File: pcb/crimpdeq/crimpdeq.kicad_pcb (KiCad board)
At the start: 2 copper layers, 23 x 63.8 mm, 48 parts, among them J2 USB4105-GF-A, J3 Loadcell_Pads, J4 Power_Sense_Pads, Q1 SS8550, Q2 DMG3415U, U1 ESP32-C3-MINI-1, U2 MCP73831T-2ACI/OT, U3 HX711, U5 MAX17048G+T10, U6 SY8088

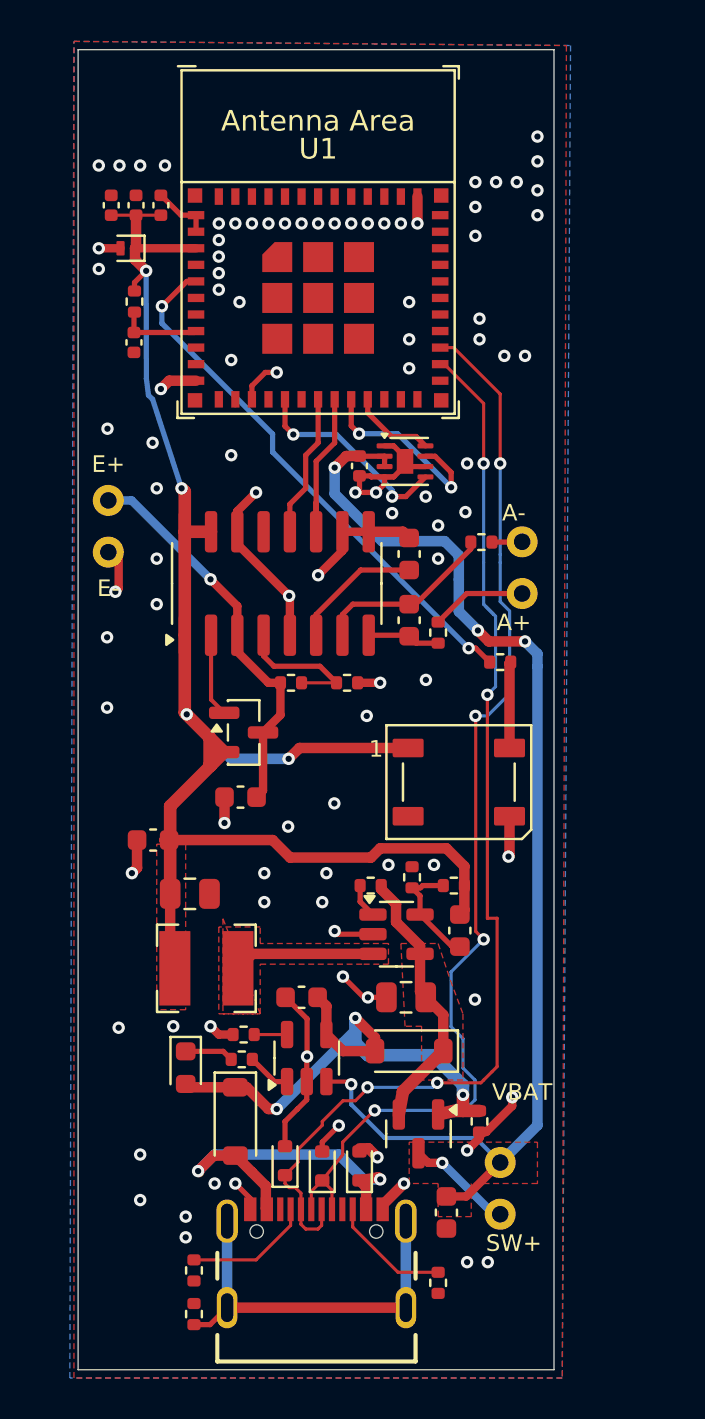
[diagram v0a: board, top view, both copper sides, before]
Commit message: Revision 3 (#26)
* Reorganize PCB designs and add crimpdeq-v2-nano (25x26mm 4-layer compact board)

Moves the original design to pcb/designs/crimpdeq-v2/ so each PCB
package can live in its own versioned directory, and adds
pcb/designs/crimpdeq-v2-nano/: a 4-layer, 25 x 26 mm redesign
(~56% smaller board area than crimpdeq-v2: 1467.4 mm2 -> 650.0 mm2)
with the ESP32 antenna and status LED both moved to the back and
USB/HX711 kept on the front.

- Electrically identical to crimpdeq-v2: same 48-component BOM,
  same 197-pad netlist, 0 changed nets
- Passes KiCad DRC (0 violations, 0 unconnected)
- Validated on JLCPCB's website DFM checker: all danger-level
  findings were reviewed and resolved before committing (functional-
  label silk-to-pad/hole clearances, tht-to-smd cable pad gaps,
  USB-C shell slot width). Only conservative warning-level advisories
  remain on the six 1.50 mm cable PTH pads and the USB shell slot
  (see reports/crimpdeq-v2-nano_jlc_tht_to_smd.md)
- Updates the CI matrix to check both designs

Physical prototype validation of antenna performance and connector
fit is still pending.

* Add agents.md and 4-layer/compact reproduction tooling, symlink CLAUDE.md

agents.md documents the frozen BOM/netlist/routing invariants and
session history for the crimpdeq-v2 / crimpdeq-v2-nano designs.
tools/4layer/ and tools/compact/ are the scripted place -> route ->
verify pipeline used to build and DFM-check crimpdeq-v2-nano from
the crimpdeq-v2 baseline. CLAUDE.md is a symlink to agents.md for
AI coding agents that look for that filename by convention.

* fix: prepare nano project for release

* test: lock corrected PCB connectivity

Validate every connected pad against the revised golden netlist so ESP32 ground-pin and pull-up regressions fail immediately.

Co-authored-by: Cursor <cursoragent@cursor.com>

* refactor: consolidate the canonical PCB package

Move shared libraries to the repository root and replace versioned design trees with the corrected prod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
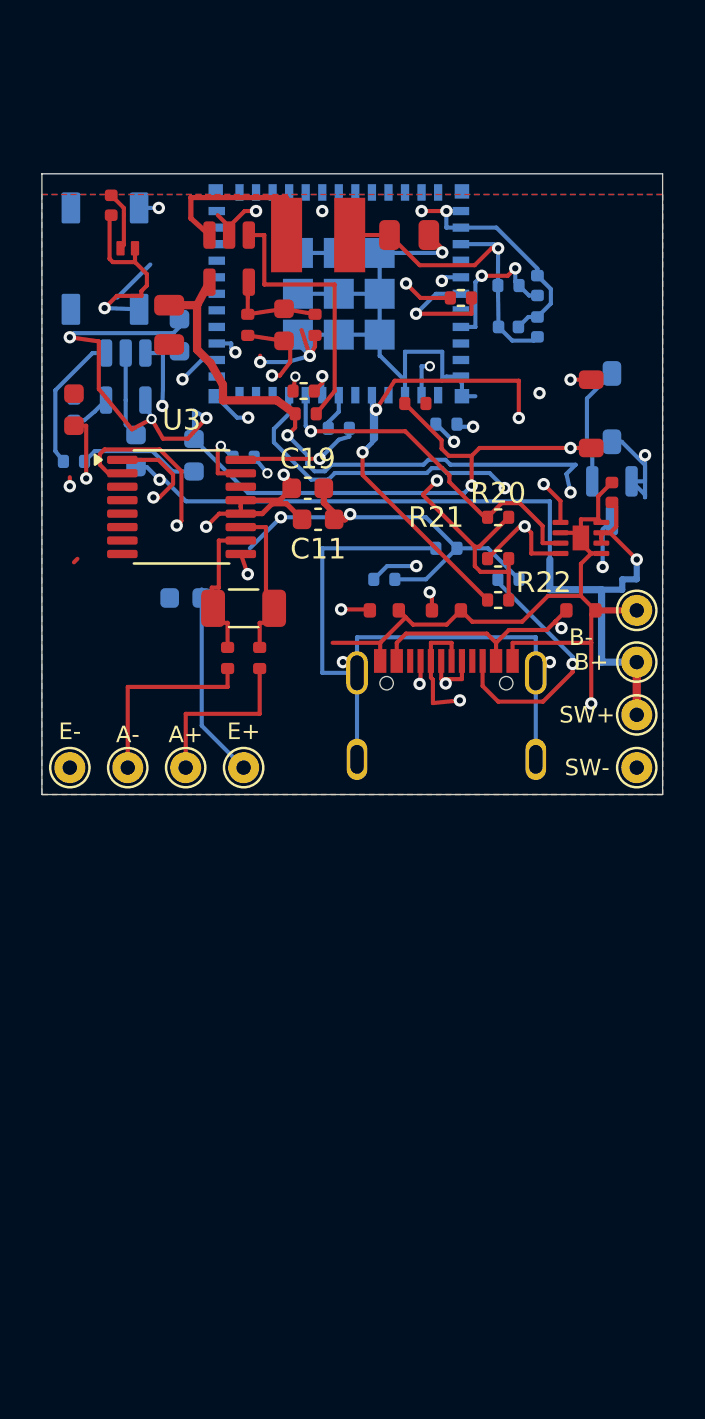
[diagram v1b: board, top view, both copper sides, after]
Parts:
- removed J3: Loadcell_Pads, External_Cable_Pads_Left
- removed J4: Power_Sense_Pads, External_Cable_Pads_Right
- removed Q1: SS8550, Package_TO_SOT_SMD:SOT-23
- removed R5: 12kR 1%, Resistor_SMD:R_0402_1005Metric
- removed R6: 8k2R 1%, Resistor_SMD:R_0402_1005Metric
- added C19: 0.1uF, Capacitor_SMD:C_0603_1608Metric, F.Cu at (140.3, 67.6)
- added J10: A-_Cable_Pad, TestPoint:TestPoint_THTPad_D1.5mm_Drill0.7mm, F.Cu at (131.6, 81.1)
- added J11: E+_Cable_Pad, TestPoint:TestPoint_THTPad_D1.5mm_Drill0.7mm, F.Cu at (137.2, 81.1)
- added J12: E-_Cable_Pad, TestPoint:TestPoint_THTPad_D1.5mm_Drill0.7mm, F.Cu at (128.8, 81.1)
- added J5: B-_Cable_Pad, TestPoint:TestPoint_THTPad_D1.5mm_Drill0.7mm, F.Cu at (156.2, 73.5)
- added J6: SW+_Cable_Pad, TestPoint:TestPoint_THTPad_D1.5mm_Drill0.7mm, F.Cu at (156.2, 78.5)
- added J7: B+_Cable_Pad, TestPoint:TestPoint_THTPad_D1.5mm_Drill0.7mm, F.Cu at (156.2, 76.0)
- added J8: SW-_Cable_Pad, TestPoint:TestPoint_THTPad_D1.5mm_Drill0.7mm, F.Cu at (156.2, 81.1)
- added J9: A+_Cable_Pad, TestPoint:TestPoint_THTPad_D1.5mm_Drill0.7mm, F.Cu at (134.4, 81.1)
- added R20: 10kR 1%, Resistor_SMD:R_0402_1005Metric, F.Cu at (149.5, 69.0)
- added R21: 10kR 1%, Resistor_SMD:R_0402_1005Metric, F.Cu at (149.5, 71.0)
- added R22: 10kR 1%, Resistor_SMD:R_0402_1005Metric, F.Cu at (149.5, 73.0)
- added R23: 47R 1%, Resistor_SMD:R_0402_1005Metric, F.Cu at (140.1, 62.9)
- added R24: 47R 1%, Resistor_SMD:R_0402_1005Metric, B.Cu at (141.8, 64.7)
- added R25: 47R 1%, Resistor_SMD:R_0402_1005Metric, F.Cu at (147.7, 58.4)
- added R26: 47R 1%, Resistor_SMD:R_0402_1005Metric, B.Cu at (137.2, 66.1)
- C1, C10, C2, C3, C5, C6, D1, D2, D4, R1, R13, R17, R18, R19, R2, R3: moved to B.Cu
- C12: footprint Capacitor_SMD:C_0603_1608Metric -> Capacitor_SMD:C_1206_3216Metric
- J2: footprint Rust_Board:GCT_USB4105-GF-A -> Crimpdeq:GCT_USB4105-GF-A
- Q2: footprint Package_TO_SOT_SMD:SOT-23 -> Crimpdeq:SOT-23; moved to B.Cu
- U1: footprint PCM_Espressif:ESP32-C3-MINI-1 -> Crimpdeq:ESP32-C3-MINI-1; moved to B.Cu
- U2: footprint Package_TO_SOT_SMD:SOT-23-5 -> Crimpdeq:MCP73831_SOT-23-5; moved to B.Cu
- U3: value HX711 -> ADS1220; footprint Package_SO:SOP-16_3.9x9.9mm_P1.27mm -> Package_SO:TSSOP-16_4.4x5mm_P0.65mm
- U6: footprint Package_TO_SOT_SMD:SOT-23-5 -> Crimpdeq:SY8088_SOT-23-5
- moved C6 39.7 mm to (132.0, 65.8), turned to 90 degrees
- moved R17 39.0 mm to (147.0, 70.5), turned to 0 degrees
- moved D8 38.3 mm to (154.0, 64.0), turned to 90 degrees
- moved L1 35.8 mm to (140.8, 55.4), turned to 0 degrees
- moved R9 34.8 mm to (145.5, 63.5), turned to 0 degrees
- moved R19 34.6 mm to (144.0, 72.0), turned to 0 degrees
- moved C15 34.5 mm to (133.6, 59.7), turned to -90 degrees
- moved R18 34.2 mm to (150.0, 72.0), turned to 0 degrees
- moved U2 34.1 mm to (131.5, 62.2), turned to -90 degrees
- moved U6 33.6 mm to (136.5, 56.5), turned to -90 degrees
- moved C17 33.6 mm to (145.2, 55.4)
- moved D2 32.6 mm to (155.0, 63.7), turned to 90 degrees
- moved C5 32.5 mm to (134.1, 60.2), turned to 90 degrees
- moved Q2 32.0 mm to (155.0, 68.2)
- moved R2 31.3 mm to (129.0, 63.8), turned to -90 degrees
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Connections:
- net /Buck_Coil renamed Buck_Coil
- net IO6_SDA renamed IO6_SCL
- net IO7_SCL renamed IO7_SDA
- C10 pad 1: E+ -> +3V3
- C11 pad 1: GND -> +3V3
- C11 pad 2: Net-(U3-VBG) -> GND
- C12 pad 1: Net-(U3-INA+) -> Net-(U3-AIN0)
- C12 pad 2: Net-(U3-INA-) -> Net-(U3-AIN1)
- R7 pad 1: Net-(U3-INA+) -> Net-(U3-AIN0)
- R8 pad 1: Net-(U3-INA-) -> Net-(U3-AIN1)
- U1 pad 13: unconnected-(U1-GPIO1/ADC1_CH1/XTAL_32K_N-Pad13) -> IO1_MISO
- U1 pad 18: IO4_DATA -> IO4_MOSI
- U1 pad 37: (no net) -> GND
- U1 pad 38: (no net) -> GND
- U1 pad 39: (no net) -> GND
- U1 pad 40: (no net) -> GND
- U1 pad 41: (no net) -> GND
- U1 pad 42: (no net) -> GND
- U1 pad 43: (no net) -> GND
- U1 pad 44: (no net) -> GND
- U1 pad 45: (no net) -> GND
- U1 pad 46: (no net) -> GND
- U1 pad 47: (no net) -> GND
- U1 pad 48: (no net) -> GND
- U1 pad 49: (no net) -> GND
- U1 pad 50: (no net) -> GND
- U1 pad 51: (no net) -> GND
- U1 pad 52: (no net) -> GND
- U1 pad 53: (no net) -> GND
- U1 pad 6: unconnected-(U1-GPIO3/ADC1_CH3-Pad6) -> IO3_CS
- U3 pad 1: +3V3 -> ADS_SCLK
- U3 pad 10: GND -> Net-(U3-AIN1)
- U3 pad 11: IO5_SCK -> Net-(U3-AIN0)
- U3 pad 12: IO4_DATA -> +3V3
- U3 pad 13: unconnected-(U3-XO-Pad13) -> +3V3
- U3 pad 14: GND -> unconnected-(U3-~{DRDY}-Pad14)
- U3 pad 15: +3V3 -> ADS_DOUT
- U3 pad 16: +3V3 -> ADS_DIN
- U3 pad 2: Net-(Q1-B) -> ADS_CS
- U3 pad 3: E+ -> GND
- U3 pad 4: Net-(U3-VFB) -> GND
- U3 pad 6: Net-(U3-VBG) -> unconnected-(U3-AIN3/REFN1-Pad6)
- U3 pad 7: Net-(U3-INA-) -> unconnected-(U3-AIN2-Pad7)
- U3 pad 8: Net-(U3-INA+) -> GND
- U3 pad 9: GND -> +3V3
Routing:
- net GND: track 63.5 -> 137.2 mm, vias 98 -> 13
- net +3V3: track 78.2 -> 116.5 mm, vias 4 -> 8
- net ADS_CS: track 0.00 -> 35.8 mm, vias 0 -> 2
- net Net-(D4-DIN): track 4.17 -> 31.1 mm, vias 0 -> 2
- net VSYS: track 13.1 -> 39.9 mm, vias 0 -> 3
- net VBUS: track 28.3 -> 53.1 mm, vias 3 -> 5
- net IO1_MISO: track 0.00 -> 24.0 mm, vias 0 -> 2
- net ADS_SCLK: track 0.00 -> 21.1 mm, vias 0 -> 2
- net IO10_ALRT: track 10.1 -> 30.0 mm, vias 2 -> 4
- net E+: track 19.9 -> 0.00 mm, vias 1 -> 0
- net IO7_SDA: track 4.10 -> 22.7 mm, vias 0 -> 2
- net Net-(J2-SHELL_GND-PadS1): track 18.9 -> 35.0 mm, vias 0 -> 2
- net IO2_LED: track 26.1 -> 10.2 mm
- net USB_D+: track 53.3 -> 37.7 mm, vias 4 -> 3
- net USB_D-: track 54.1 -> 40.2 mm, vias 4 -> 3
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- added copper zone on In2.Cu, net +3V3
- added copper zone on In1.Cu, net GND
- removed copper zone on F.Cu, net +3V3
- removed copper zone on F.Cu, net +BATT
- removed copper zone on F.Cu, net Buck_Coil
- removed copper zone on F.Cu, net VSYS
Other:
- board size 23 x 63.8 mm -> 30 x 30 mm
- copper layers 2 -> 4
- board text added: "A+"
- board text added: "A-"
- board text added: "B+"
- board text added: "B-"
- board text added: "E+"
- board text added: "E-"
- board text added: "SW+"
- board text added: "SW-"
